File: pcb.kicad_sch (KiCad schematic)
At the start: 48 parts, among them J1 USB_B_Mini, J2 Conn_ARM_JTAG_SWD_20, J3 Micro_SD_Card_Det1, J4 Conn_02x25_Odd_Even, J5 Conn_02x25_Odd_Even, SW1 SW_RESET, U1 STM32H750VBTx, U2 USBLC6-2P6, U3 TLV1117-33, Y2 25MHz 9uF

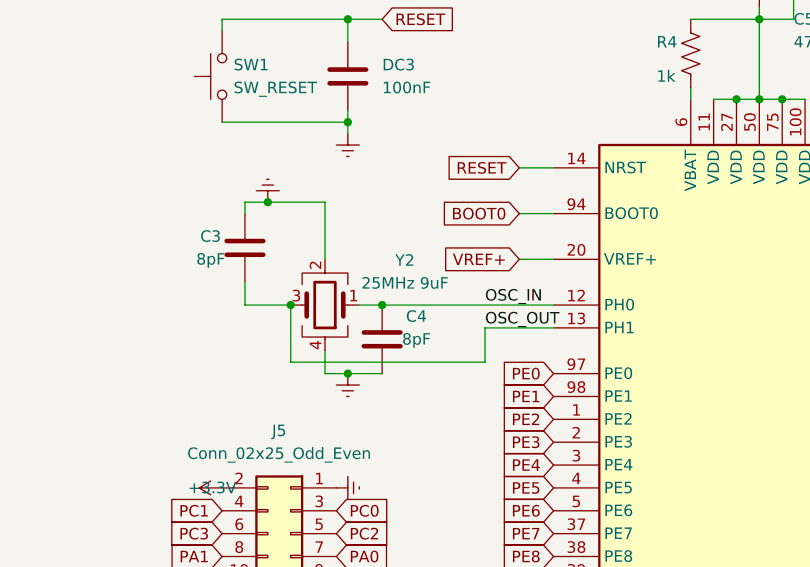
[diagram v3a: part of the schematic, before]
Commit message: PCB: Updated footprint of JTAG connector
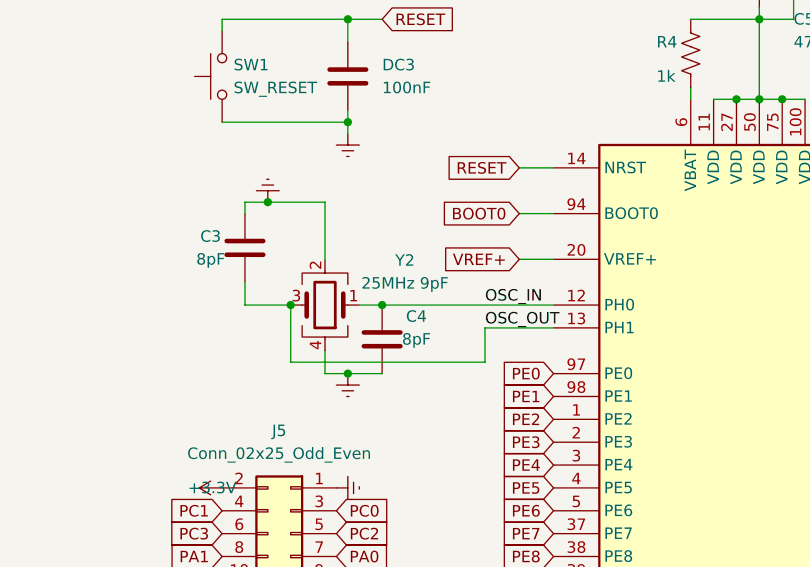
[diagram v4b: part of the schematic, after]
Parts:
- J2: footprint Connector_TE-Connectivity:TE_MATE-N-LOK_1-794070-x_2x10_P4.14mm_Vertical -> Connector_PinSocket_2.54mm:PinSocket_2x10_P2.54mm_Vertical
- L1, L2: footprint Inductor_SMD:L_0402_1005Metric -> Inductor_SMD:L_0603_1608Metric
- Y2: value 25MHz 9uF -> 25MHz 9pF
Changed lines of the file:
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@@
   (title_block
     (title "top")
-    (rev "1.1")
-    (comment 1 "First version, using swd, no gpio connector")
+    (rev "1.2")
+    (comment 1 "First version")
   )
   (junction (at 163.83 15.24) (diameter 0) (color 0 0 0 0)
@@
       (effects (font (size 1.27 1.27)))
     )
-    (property "Footprint" "Inductor_SMD:L_0402_1005Metric" (at 19.685 76.2 0)
+    (property "Footprint" "Inductor_SMD:L_0603_1608Metric" (at 19.685 76.2 0)
       (effects (font (size 1.27 1.27)) hide)
     )
@@
       (effects (font (size 1.27 1.27)) (justify right))
     )
-    (property "Footprint" "Connector_TE-Connectivity:TE_MATE-N-LOK_1-794070-x_2x10_P4.14mm_Vertical" (at 38.1 64.77 0)
+    (property "Footprint" "Connector_PinSocket_2.54mm:PinSocket_2x10_P2.54mm_Vertical" (at 38.1 64.77 0)
       (effects (font (size 1.27 1.27)) (justify left top) hide)
     )
@@
       (effects (font (size 1.27 1.27)))
     )
-    (property "Value" "25MHz 9uF" (at 99.06 48.3869 0)
+    (property "Value" "25MHz 9pF" (at 99.06 48.3869 0)
       (effects (font (size 1.27 1.27)))
     )
@@
     )
     (pin "1")
-    (pin "4")
     (pin "2")
     (pin "3")
+    (pin "4")
     (instances
       (project "pcb"
@@
       (effects (font (size 1.27 1.27)))
     )
-    (property "Footprint" "Inductor_SMD:L_0402_1005Metric" (at 264.795 106.68 0)
+    (property "Footprint" "Inductor_SMD:L_0603_1608Metric" (at 264.795 106.68 0)
       (effects (font (size 1.27 1.27)) hide)
     )

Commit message: BOM: Updates BOM to remove out of stock parts, switched out reset switch, new footprint SPST-NO 3.5x6.0mm, moved it away from connector due to it's higher profile
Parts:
- SW1: footprint Button_Switch_SMD:SW_SPST_CK_RS282G05A3 -> Button_Switch_SMD:SW_Tactile_SPST_NO_Straight_CK_PTS636Sx25SMTRLFS
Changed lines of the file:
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@@
   (title_block
     (title "top")
-    (rev "1.2")
+    (rev "1.3")
     (comment 1 "First version")
   )
@@
       (effects (font (size 1.27 1.27)) (justify right))
     )
-    (property "Footprint" "Button_Switch_SMD:SW_SPST_CK_RS282G05A3" (at 73.66 25.4 0)
-      (effects (font (size 1.27 1.27)) hide)
-    )
+    (property "Footprint" "Button_Switch_SMD:SW_Tactile_SPST_NO_Straight_CK_PTS636Sx25SMTRLFS" (at 73.66 25.4 0)
+      (effects (font (size 1.27 1.27)) hide)
+    )
